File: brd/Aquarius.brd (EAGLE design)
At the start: 75.5 x 129 mm, 35 parts, among them IC1 74123D, J2 DS18B20, J4 GSM/GPS, U1 DHT22, U2 DS3231SN, X1 Conn BNC : pH, X2 Conn BNC : Dissolved Oxygen, X3 Conn BNC : Conductivity

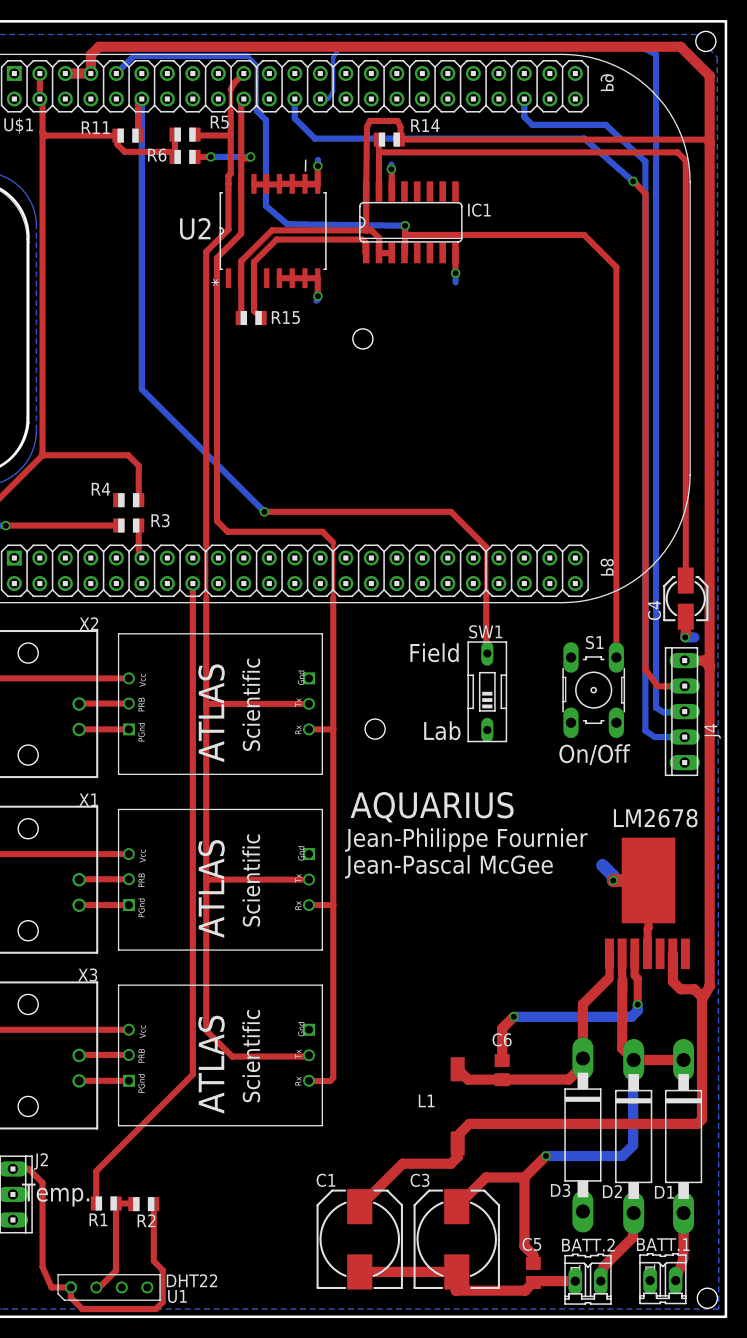
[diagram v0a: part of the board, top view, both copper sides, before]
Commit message: PCB update
Changed connectors for battery input
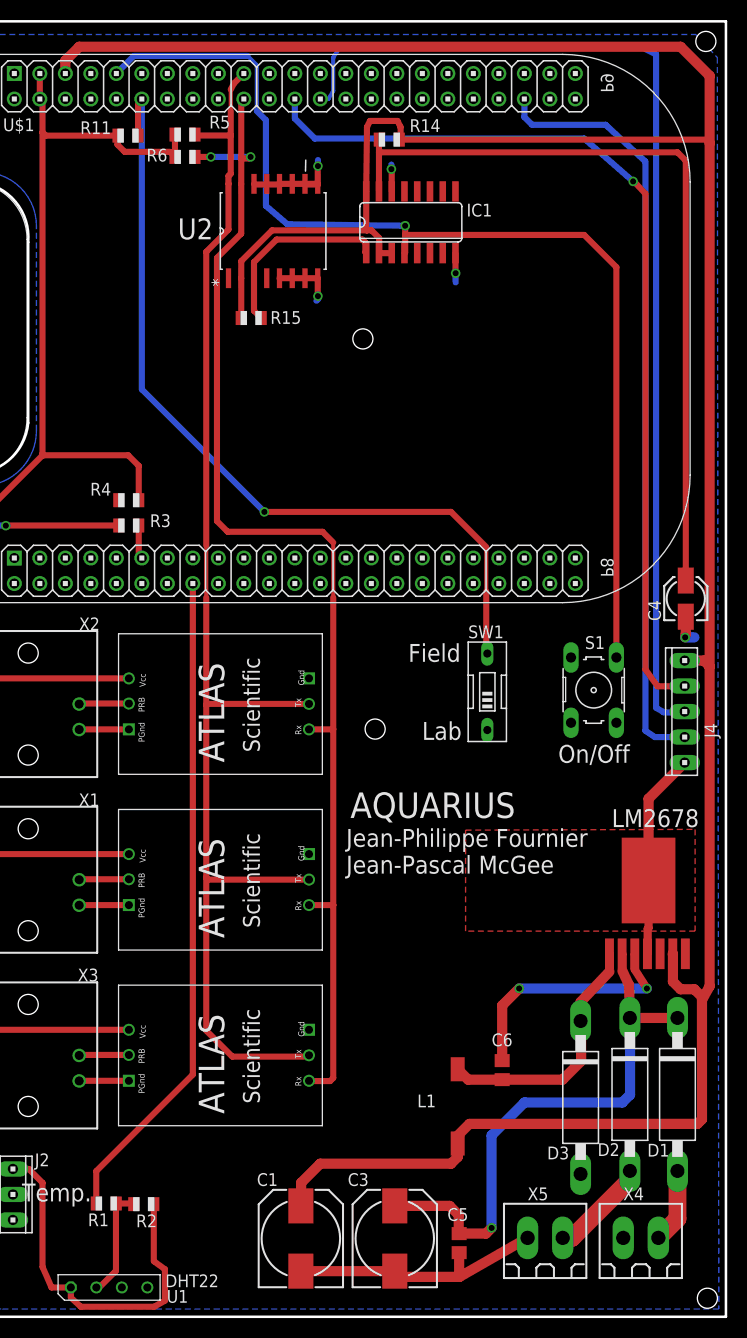
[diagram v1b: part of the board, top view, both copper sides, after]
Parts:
- removed BATT.1, BATT.2: (no value), con-amp-quick:02P
- added X4: Batt.1, con-weidmueller-sl35:180G-2
- added X5: Batt.2, con-weidmueller-sl35:180G-2
- moved C5 7.97 mm to (8.43, -51.2)
- moved C3 6.17 mm to (2.01, -50.7)
- moved C1 5.87 mm to (-7.34, -50.7)
- moved D1 4.24 mm to (30.2, -36.4)
- moved D2 4.21 mm to (25.4, -36.4)
- moved D3 3.74 mm to (20.5, -36.7)
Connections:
- new net SYS_5V: U$1.53
- net 5V: no longer U$1.53
- net GND: now also X4.1, X5.1; no longer BATT.1.1, BATT.2.1
- net N$2: now also X4.2; no longer BATT.1.2
- net N$8: now also X5.2; no longer BATT.2.2
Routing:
- net GND: track 61.9 -> 73.0 mm, vias 6 -> 5
- net 5V: track 290.5 -> 297.4 mm
- net N$10: track 53.7 -> 55.7 mm
- net N$8: track 8.05 -> 9.98 mm
- net N$9: track 23.2 -> 24.4 mm
- net N$2: track 6.86 -> 7.46 mm
- added copper zone on layer 1, net GND

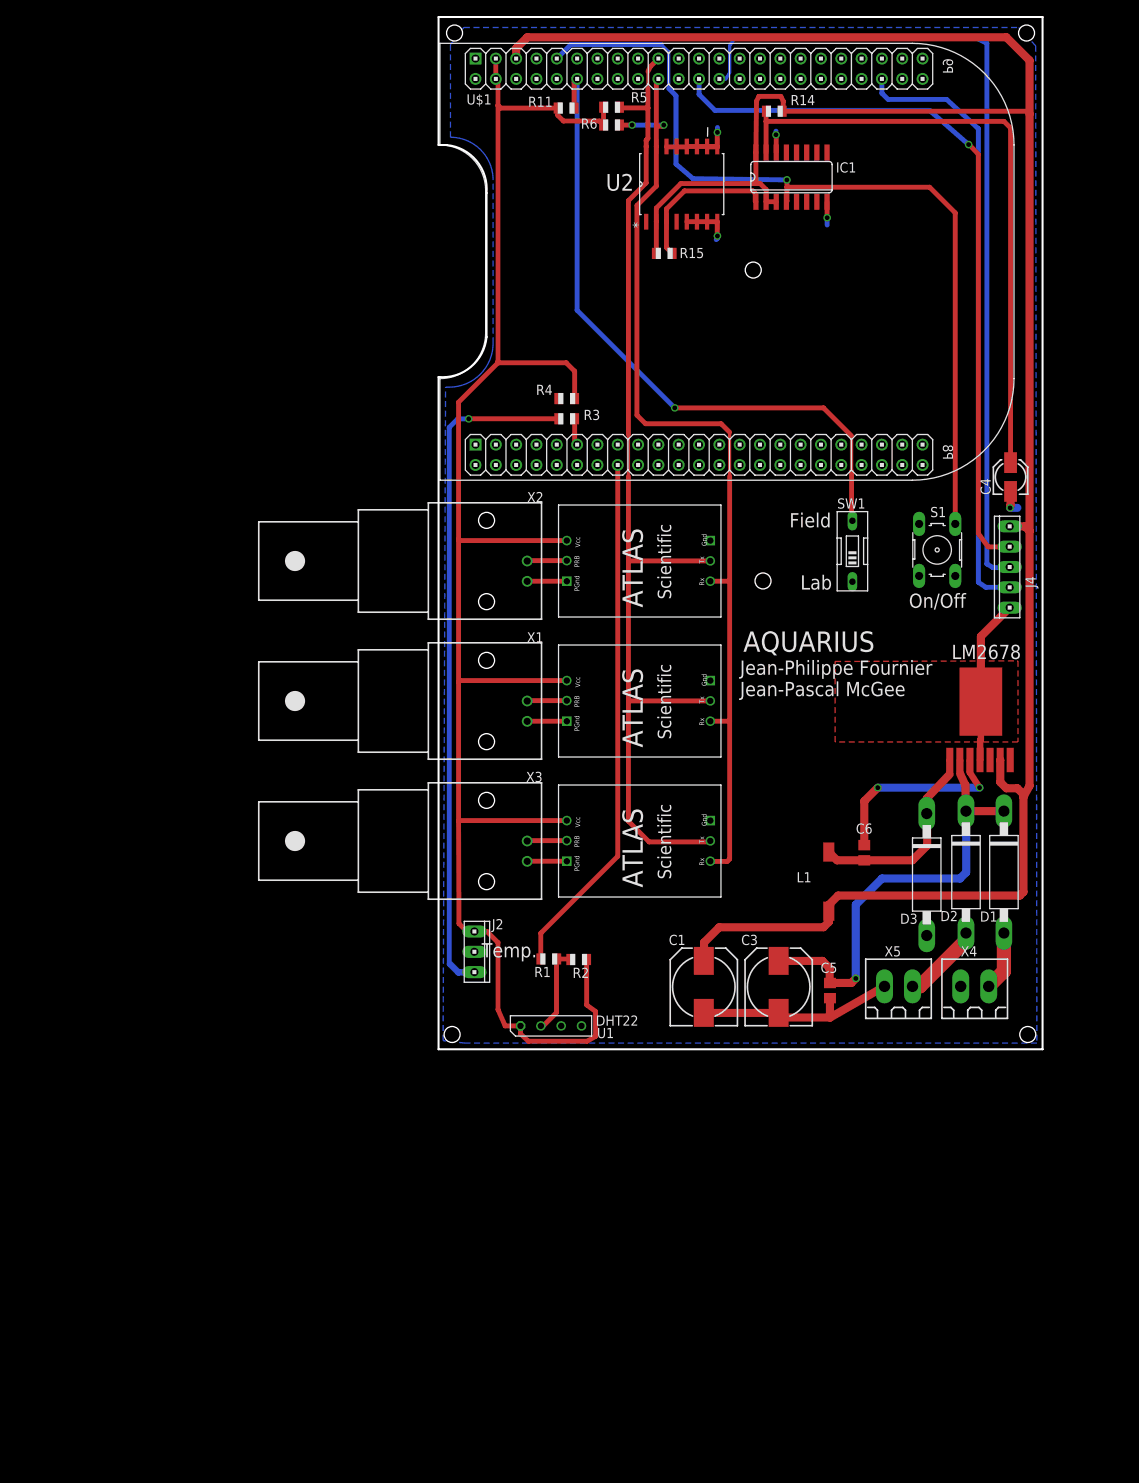
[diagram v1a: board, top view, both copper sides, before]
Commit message: PCB Update and modified name of Atlas driver cpp's
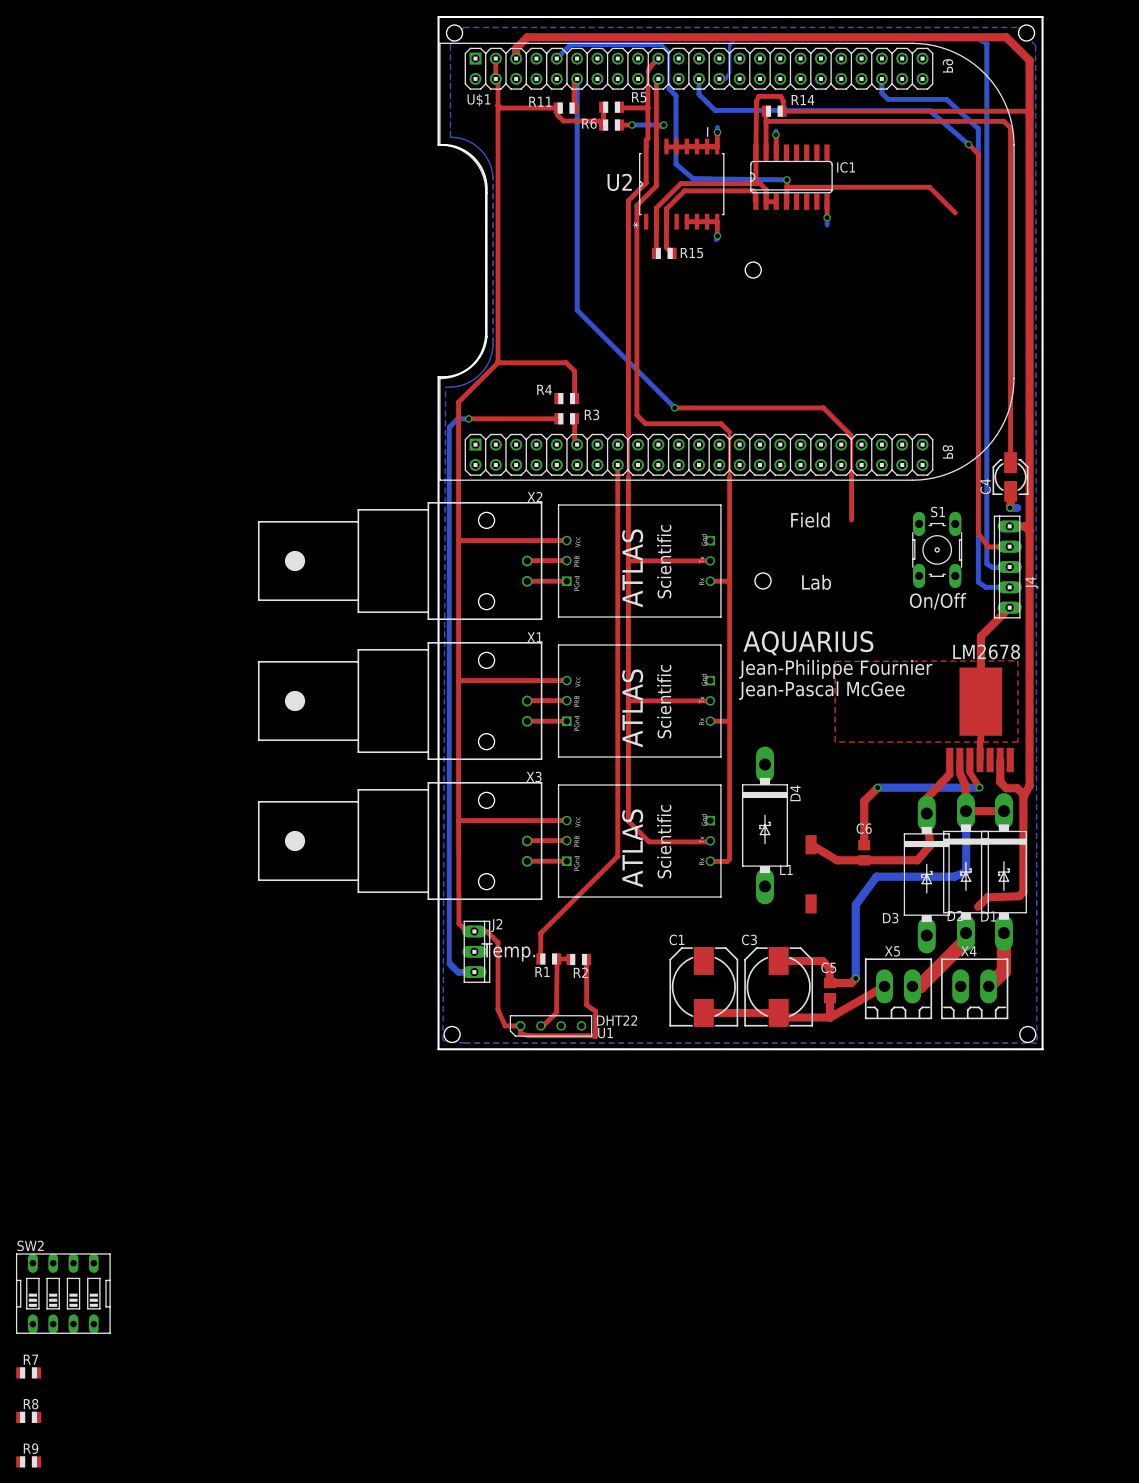
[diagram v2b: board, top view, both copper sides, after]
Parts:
- removed SW1: (no value), special:EDG-01
- added D4: (no value), diode:DO201T15
- added DRILEGEND: (no value), drilegend:DRILEGEND
- added R7, R8, R9: 4.7K, adafruit:R0805
- added SW2: (no value), special:EDG-04
- D1, D2, D3: device adafruit:CB417-15 -> diode:DO201T15
- moved L1 2.39 mm to (6.07, -36.7)
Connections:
- new net N$16: C1.+, D4.A, L1.2
- new net N$18: R11.1, SW2.8, U$1.58
- new net N$19: R8.1, SW2.6, U$1.30
- new net N$21: R9.1, SW2.5, U$1.28
- net 5V: now also D4.C; no longer C1.+, L1.2
- net GND: no longer SW1.1
- net INT: now also S1.1
- net N$7: now also R7.1, SW2.7, U$1.40; no longer R11.1, SW1.2, U$1.58
- net PWR_BUT: no longer S1.1
- net VCC: now also R7.2, R8.2, R9.2
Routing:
- net N$7: track 84.2 -> 0.00 mm, vias 1 -> 0
- net N$18: track 0.00 -> 83.5 mm, vias 0 -> 1
- net 5V: track 297.4 -> 257.6 mm
- net PWR_BUT: track 108.0 -> 69.2 mm
- net N$13: track 25.4 -> 28.1 mm
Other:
- board text added: "01-16"
- board text added: "01-20"
- board text added: "LAYER-STACK"

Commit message: PCB JayMcGee Version
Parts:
- moved R9 159.3 mm to (13.6, 9.37), turned to 90 degrees
- moved R8 153.4 mm to (11.0, 9.37), turned to 90 degrees
- moved R7 147.6 mm to (8.53, 9.37), turned to 90 degrees
- moved SW2 132.9 mm to (9.75, 1.68)
- moved DRILEGEND 23.1 mm to (-40.5, -64.9)
- moved C6 12.5 mm to (18.6, -22.9), turned to 180 degrees
- moved D4 12.2 mm to (11.2, -36.1)
- moved D3 2.94 mm to (17.6, -36.2)
- moved C5 1.91 mm to (8.96, -53.0)
- moved L1 1.85 mm to (4.24, -36.4)
- moved X5 1.37 mm to (15.6, -50.7)
- moved D2 1.33 mm to (24.1, -36.1)
- moved X4 1.14 mm to (25.4, -50.7)
- moved D1 0.49 mm to (30.6, -36.1)
- moved C3 0.46 mm to (2.47, -50.7)
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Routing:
- net INT: track 19.1 -> 80.7 mm, vias 0 -> 1
- net VCC: track 220.5 -> 266.1 mm, vias 0 -> 2
- net N$21: track 0.00 -> 31.1 mm
- net N$16: track 0.00 -> 26.5 mm
- net PWR_BUT: track 69.2 -> 43.1 mm
- net N$19: track 0.00 -> 25.5 mm
- net GND: track 73.0 -> 95.4 mm, vias 5 -> 3
- net I2C2_SDA: track 122.9 -> 138.0 mm, vias 2 -> 0
- net N$7: track 0.00 -> 14.8 mm, vias 0 -> 1
- net 5V: track 257.6 -> 243.2 mm, vias 0 -> 1
- net N$9: track 24.4 -> 11.0 mm
- net RX: track 105.9 -> 94.9 mm
- net N$6: track 65.7 -> 76.0 mm, vias 0 -> 2
- net I2C2_SCL: track 132.4 -> 123.4 mm, vias 0 -> 2
- net P: track 76.4 -> 80.8 mm
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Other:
- board text removed: "Jean-Philippe Fournier Jean-Pascal McGee"

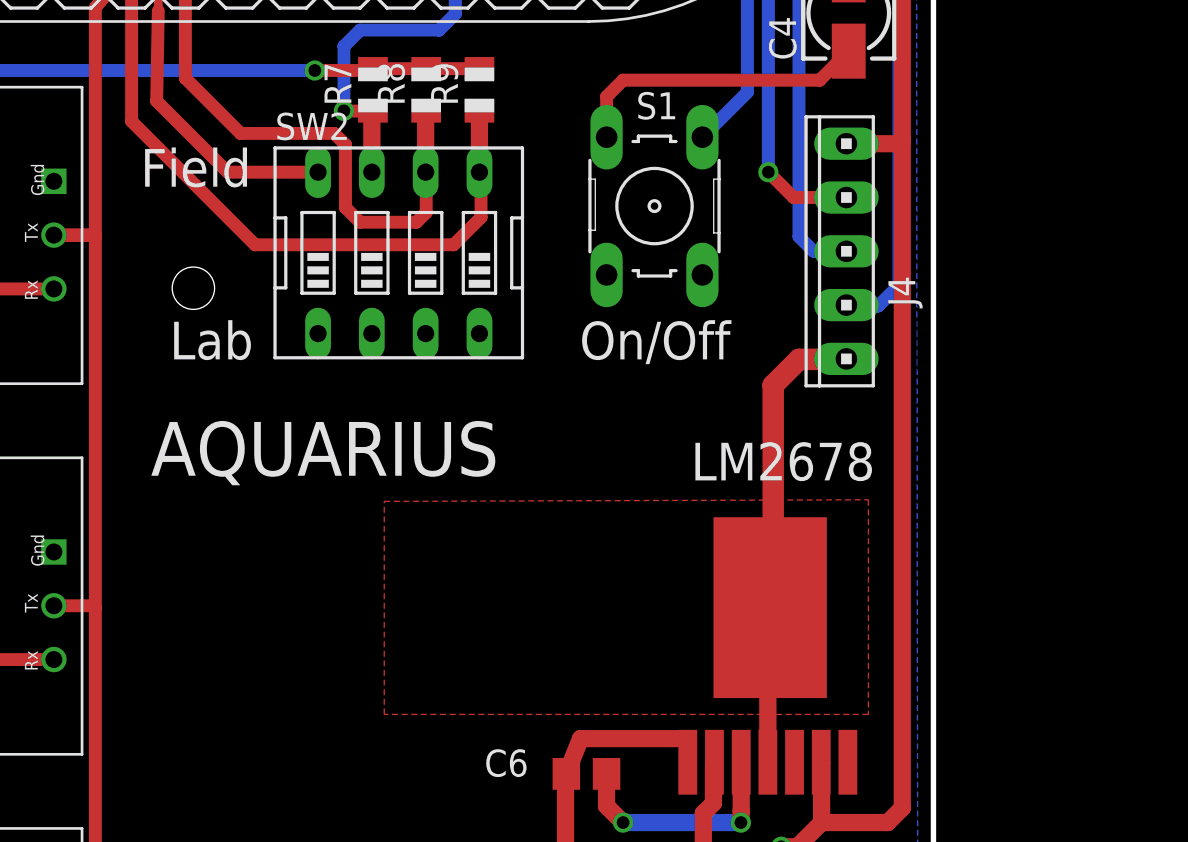
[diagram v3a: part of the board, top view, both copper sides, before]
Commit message: Ajout de ground sur le schema
Préparation a une 2eime version du PCB
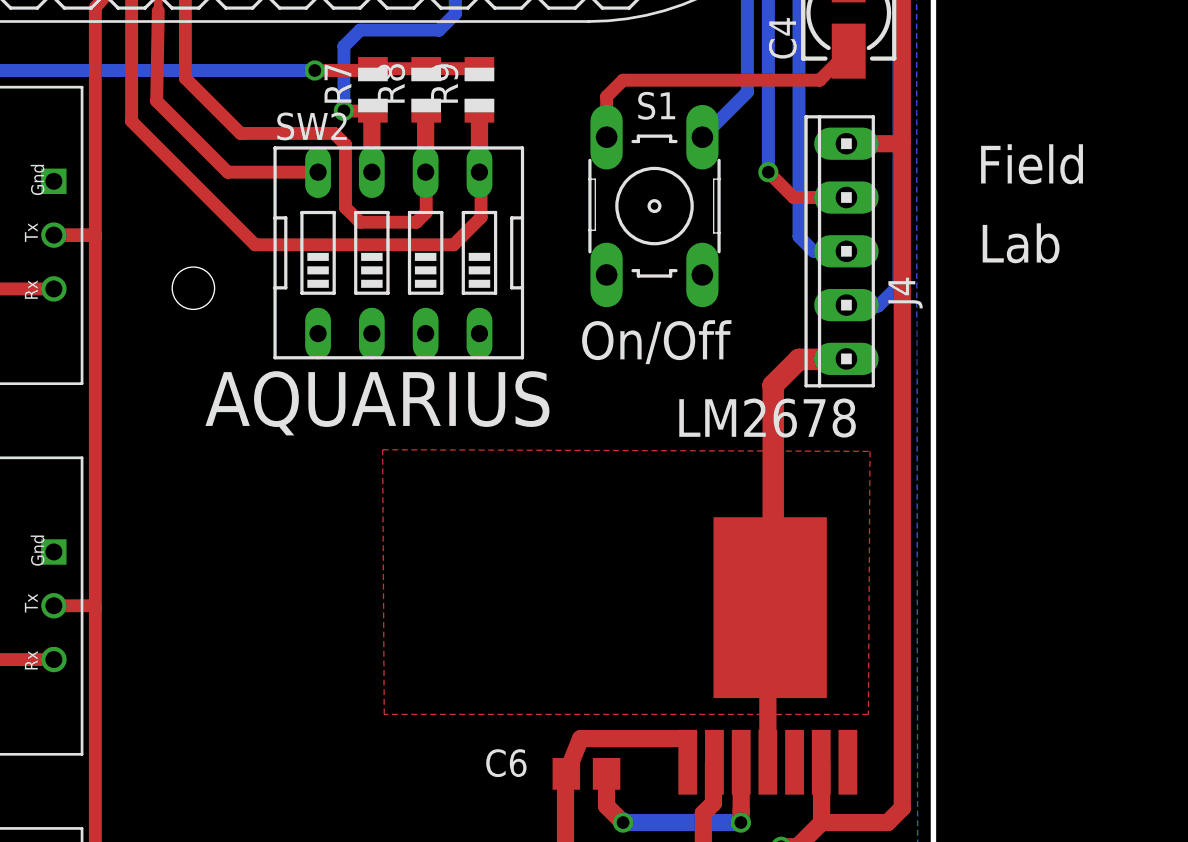
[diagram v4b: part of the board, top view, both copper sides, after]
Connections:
- removed net N$1: U$1.52
- net 5V: now also U$1.52
- net GND: now also SW2.1, SW2.2, SW2.3, SW2.4
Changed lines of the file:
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@@
 <?xml version="1.0" encoding="utf-8"?>
 <!DOCTYPE eagle SYSTEM "eagle.dtd">
-<eagle version="7.1.0">
+<eagle version="6.4">
 <drawing>
 <settings>
@@
 <layer number="27" name="tValues" color="7" fill="1" visible="yes" active="yes"/>
 <layer number="28" name="bValues" color="7" fill="1" visible="yes" active="yes"/>
-<layer number="29" name="tStop" color="7" fill="3" visible="no" active="yes"/>
+<layer number="29" name="tStop" color="7" fill="3" visible="yes" active="yes"/>
 <layer number="30" name="bStop" color="7" fill="6" visible="no" active="yes"/>
 <layer number="31" name="tCream" color="7" fill="4" visible="no" active="yes"/>
@@
 <wire x1="-39.5" y1="54.5" x2="-40.5" y2="54.5" width="0.254" layer="20"/>
 <wire x1="-40.5" y1="54.5" x2="-40.5" y2="70.5" width="0.254" layer="20"/>
-<text x="-1.9548" y="-8.8468" size="2.54" layer="21">AQUARIUS</text>
+<text x="17.0424" y="-3.9548" size="2.54" layer="21" rot="R180">AQUARIUS</text>
 <hole x="-38.8048" y="-56.6848" drill="2"/>
 <hole x="33.1524" y="-56.6848" drill="2"/>
@@
 <hole x="-1.162" y="38.87" drill="2"/>
 <text x="18.288" y="-3.3528" size="1.778" layer="25">On/Off</text>
-<text x="-2.4384" y="4.8006" size="1.778" layer="25">Field</text>
-<text x="-1.0668" y="-3.3528" size="1.778" layer="25">Lab</text>
+<text x="37.0332" y="4.953" size="1.778" layer="25">Field</text>
+<text x="37.1094" y="1.2192" size="1.778" layer="25">Lab</text>
 <text x="-27.051" y="-44.2722" size="1.778" layer="25" rot="R180">Temp.</text>
-<text x="23.5458" y="-9.0678" size="1.778" layer="25">LM2678</text>
+<text x="22.7838" y="-7.0104" size="1.778" layer="25">LM2678</text>
 <text x="-58.5046" y="-64.2704" size="1.778" layer="144">LAYER-STACK</text>
 <text x="-79.8914" y="-70.6331" size="1.778" layer="145">01-16</text>
@@
 <wire x1="-33.992" y1="-26.912" x2="-35.008" y2="-27.928" width="0.1016" layer="146"/>
 <wire x1="-34.5" y1="-26.912" x2="-34.5" y2="-27.928" width="0.1016" layer="146"/>
+<rectangle x1="8.8392" y1="-20.3454" x2="32.1564" y2="-7.4676" layer="29"/>
 </plain>
 <attributes>
@@
 <pass name="Default">
 <param name="RoutingGrid" value="50mil"/>
-<param name="AutoGrid" value="1"/>
-<param name="Efforts" value="0"/>
-<param name="TopRouterVariant" value="1"/>
 <param name="tpViaShape" value="round"/>
 <param name="PrefDir.1" value="|"/>
@@
 <contactref element="X5" pad="1"/>
 <polygon width="1.016" layer="1">
-<vertex x="9.0678" y="-10.0584"/>
-<vertex x="31.9278" y="-9.9822"/>
+<vertex x="8.9916" y="-7.62"/>
+<vertex x="32.004" y="-7.6962"/>
 <vertex x="31.9278" y="-20.1168"/>
 <vertex x="9.0678" y="-20.1168"/>
@@
 <wire x1="-12.0396" y1="54.3306" x2="-12.0396" y2="56.9214" width="0.6096" layer="1"/>
 <via x="-12.0396" y="56.9214" extent="1-16" drill="0.6" shape="square"/>
+<contactref element="SW2" pad="1"/>
+<contactref element="SW2" pad="2"/>
+<contactref element="SW2" pad="3"/>
+<contactref element="SW2" pad="4"/>
 </signal>
 <signal name="N$3">
@@
 <wire x1="-0.8302" y1="53.5598" x2="-0.8302" y2="49.4618" width="0.6096" layer="1"/>
 <wire x1="-0.8302" y1="49.4618" x2="-0.8382" y2="49.3014" width="0.6096" layer="1"/>
+<contactref element="U$1" pad="52"/>
+<wire x1="-30.8" y1="65.305" x2="-30.8" y2="62.765" width="0" layer="19" extent="1-1"/>
 </signal>
 <signal name="PWR_BUT">
@@
 <contactref element="U2" pad="4"/>
 </signal>
-<signal name="N$1">
-<contactref element="U$1" pad="52"/>
-</signal>
 <signal name="N$2">
